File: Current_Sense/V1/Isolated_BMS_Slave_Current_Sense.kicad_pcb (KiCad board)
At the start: 2 copper layers, 0 parts

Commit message: placing power supply
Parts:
- added C201: 885012107015, Capacitors:C0805, F.Cu at (-25.4, -1.42)
- added C202, C205, C209, C301, C305, C306, C510, C514: 885012207098, Capacitors:C0805, F.Cu at (-25.4, -1.42)
- added C203, C204, C208: 885012207102, Capacitors:C0805, F.Cu at (-25.4, -1.42)
- added C206, C207, C302, C303, C310, C311: Capacitor_Generic, Capacitors:C0805, F.Cu at (-25.4, -1.42)
- added C304, C307, C308, C309: 885012207080, Capacitors:C0805, F.Cu at (-25.4, -1.42)
- added C401: C3216X5R1E336M160AC, Capacitors:C1206, B.Cu at (189.1, 68.8)
- added C402: C3216X5R1E336M160AC, Capacitors:C1206, B.Cu at (186.4, 68.8)
- added C403: C3216X5R1E336M160AC, Capacitors:C1206, B.Cu at (183.8, 68.8)
- added C404: C3216X5R1E336M160AC, Capacitors:C1206, F.Cu at (193.0, 93.9)
- added C405: C3216X5R1E336M160AC, Capacitors:C1206, F.Cu at (193.0, 91.1)
- added C406: C3216X5R1E336M160AC, Capacitors:C1206, B.Cu at (193.0, 92.5)
- added C407: C3216X5R1E336M160AC, Capacitors:C1206, B.Cu at (196.5, 84.5)
- added C408: C3216X5R1E336M160AC, Capacitors:C1206, B.Cu at (189.1, 63.3)
- added C409: C3216X5R1E336M160AC, Capacitors:C1206, B.Cu at (186.4, 63.3)
- added C410: C3216X5R1E336M160AC, Capacitors:C1206, B.Cu at (183.8, 63.3)
- added C411: 885012207098, Capacitors:C0805, B.Cu at (188.3, 83.6)
- added C412: 885012107018, Capacitors:C0805, F.Cu at (179.1, 92.6)
- added C413: 885012107018, Capacitors:C0805, F.Cu at (179.1, 90.0)
- added C414: 885012107014, Capacitors:C0805, F.Cu at (179.1, 87.2)
- added C415: 885012107018, Capacitors:C0805, F.Cu at (173.0, 69.8)
- added C416: 885012107018, Capacitors:C0805, F.Cu at (175.5, 69.8)
- added C417: 885012107014, Capacitors:C0805, F.Cu at (166.1, 74.7)
- added C418, C419: 885012107018, Capacitors:C0805, F.Cu at (-25.4, -1.42)
- added C420: 885012107014, Capacitors:C0805, F.Cu at (-25.4, -1.42)
- added C501: 885012007027, Capacitors:C0805, F.Cu at (57.3, 95.6)
- added C502: 885012007027, Capacitors:C0805, F.Cu at (66.2, 97.8)
- added C503: 885012207098, Capacitors:C0805, B.Cu at (71.2, 111.6)
- added C504: 885012107015, Capacitors:C0805, B.Cu at (70.5, 114.2)
- added C505: 885012007053, Capacitors:C0805, F.Cu at (32.3, 103.9)
- added C506: 885012007053, Capacitors:C0805, F.Cu at (32.3, 91.8)
- added C507: 885012207098, Capacitors:C0805, B.Cu at (79.9, 113.1)
- added C508: 885012107015, Capacitors:C0805, B.Cu at (65.7, 118.6)
- added C509: 885012207092, Capacitors:C0805, B.Cu at (68.1, 118.6)
- added C511: 885012107018, Capacitors:C0805, B.Cu at (77.2, 125.6)
- added C512: 885012207098, Capacitors:C0805, B.Cu at (79.2, 123.3)
- added C513: 885012207098, Capacitors:C0805, B.Cu at (71.6, 123.6)
- added C515: 885012007053, Capacitors:C0805, F.Cu at (-25.4, -1.42)
- added D301, D302: D1213A-02SOL-7, IC:SOT-23-3, F.Cu at (-25.4, -1.42)
- added D401: NSR0530HT1G, Diodes:SOD-323, F.Cu at (188.8, 80.2)
- added D501: 150080VS75000, Diodes:LED_0805_GREEN, F.Cu at (66.8, 134.6)
- added D502: 150080YS75000, Diodes:LED_0805_YELLOW, F.Cu at (71.6, 134.5)
- added D503: 150080RS75000, Diodes:LED_0805_RED, F.Cu at (77.1, 134.5)
- added J201: 649002227222, Connectors:649002227222, F.Cu at (47.2, 85.2)
- added J202: 649002227222, Connectors:649002227222, F.Cu at (86.7, 84.8)
- added J301: 649006227222, Connectors:649006227222, F.Cu at (196.1, 110.5)
- added J302: 649006227222, Connectors:649006227222, F.Cu at (175.8, 110.5)
- added J401: Header_Male_Pin_2.54mm_1X2_,_Unshrouded, Connectors:Headers_2.54mm_1X2, F.Cu at (-25.4, -1.42)
- added J501: Header_Male_Pin_2.54mm_1X6_,_Unshrouded, Connectors:Headers_2.54mm_1X6, F.Cu at (-25.4, -1.42)
- added J502: Header_Male_Pin_2.54mm_1X3_,_Unshrouded, Connectors:Headers_2.54mm_1X3, F.Cu at (-25.4, -1.42)
- added L401: LQM31PN4R7M00L, Inductors:I1206, F.Cu at (185.9, 71.4)
- added L402: LQM31PN4R7M00L, Inductors:I1206, F.Cu at (193.0, 88.3)
- added L403: LQM31PN4R7M00L, Inductors:I1206, F.Cu at (186.0, 66.3)
- added R201: RC0805JR-072K2L, Resistors:R0805, F.Cu at (-25.4, -1.42)
- added R202, R203, R213: RC0805JR-0747KL, Resistors:R0805, F.Cu at (-25.4, -1.42)
- added R204: RC0805JR-0733KL, Resistors:R0805, F.Cu at (-25.4, -1.42)
- added R205, R206, R212: RC0805JR-0722RL, Resistors:R0805, F.Cu at (-25.4, -1.42)
- added R207, R210: Resistor_Generic, Capacitors:C0805, F.Cu at (-25.4, -1.42)
- added R208, R209, R211, R302, R303, R305, R306, R504, R506: RC0805JR-07100RL, Resistors:R0805, F.Cu at (-25.4, -1.42)
- added R301, R307: RC0805JR-070RL, Resistors:R0805, F.Cu at (-25.4, -1.42)
- added R304: RC1206JR-07120RL, Resistors:R1206, F.Cu at (-25.4, -1.42)
- added R401: Resistor_Generic, Resistors:R0805, B.Cu at (176.0, 69.8)
- added R402: RC0805JR-071KL, Resistors:R0805, B.Cu at (190.4, 79.0)
- added R403: Resistor_Generic, Resistors:R0805, B.Cu at (176.0, 63.4)
- added R501: RC0805JR-070RL, Resistors:R0805, F.Cu at (61.8, 100.6)
- added R502: RC0805JR-070RL, Resistors:R0805, F.Cu at (40.1, 99.8)
- added R503, R505, R507: RC0805JR-074K7L, Resistors:R0805, F.Cu at (-25.4, -1.42)
- added R508: RC0805JR-07470RL, Resistors:R0805, F.Cu at (66.8, 138.8)
- added R509: RC0805JR-07470RL, Resistors:R0805, F.Cu at (71.6, 138.7)
- added R510: RC0805JR-07470RL, Resistors:R0805, F.Cu at (77.1, 138.7)
- added R511: RC0805JR-071KL, Resistors:R0805, F.Cu at (-25.4, -1.42)
- added SW501: PTS645SM43SMTR92, Switches:PTS645_6X6X4_SMD, F.Cu at (36.4, 135.0)
- added SW502: PTS645SM43SMTR92, Switches:PTS645_6X6X4_SMD, F.Cu at (52.7, 135.3)
- added TP201, TP202, TP203, TP204, TP301, TP302, TP303, TP304, TP407, TP501, TP502, TP503: Test_Point_THM, Connectors:Keystone_5001, F.Cu at (-25.4, -1.42)
- added TP401: Test_Point_THM, Connectors:Keystone_5001, F.Cu at (180.5, 71.9)
- added TP402: Test_Point_THM, Connectors:Keystone_5001, F.Cu at (199.4, 88.3)
- added TP403: Test_Point_THM, Connectors:Keystone_5001, F.Cu at (180.5, 67.7)
- added TP404: Test_Point_THM, Connectors:Keystone_5001, F.Cu at (186.3, 103.1)
- added TP405: Test_Point_THM, Connectors:Keystone_5001, F.Cu at (171.2, 88.4)
- added TP406: Test_Point_THM, Connectors:Keystone_5001, F.Cu at (162.6, 66.0)
- added TP408: Test_Point_THM, Connectors:Keystone_5001, F.Cu at (180.5, 63.4)
- added U201: LM4040CYM3-4.1-TR, IC:SOT-23-3, F.Cu at (-25.4, -1.42)
- added U202: PGA281AIPWR, IC:TSSOP-16, F.Cu at (75.4, 93.6)
- added U203: ADC141S626CIMM/NOPB, IC:VSSOP-10, F.Cu at (74.8, 100.7)
- added U301: SI8422AB-D-IS, IC:SOIC-8, F.Cu at (168.5, 82.8)
- added U302: SN65HVD232DR, IC:SOIC-8, F.Cu at (178.7, 82.9)
- added U401: PQMC3-D12-D15-S, Assembly:PQMC3, F.Cu at (193.2, 84.1)
- added U402: NCP1117LPST33T3G, IC:SOT-223-3, B.Cu at (178.1, 89.9)
- added U403: NCP1117ST50T3G, IC:SOT-223-3, F.Cu at (168.1, 68.8)
- added U404: NCP1117LPST33T3G, IC:SOT-223-3, F.Cu at (175.0, 33.0)
- added U501: STM32F446RE, IC:LQFP-64, F.Cu at (74.0, 117.5)
- added XTAL501: ABS25-32.768KHZ-6-T, Crystals:ABS25, F.Cu at (61.7, 95.0)
- added XTAL502: ABLS-8.000MHZ-D-T, Crystals:HC49_US, F.Cu at (36.1, 96.8)

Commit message: remove NTC, place component on PCB
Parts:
- removed J201: 649002227222, Connectors:649002227222
- C201, C202, C203, C204, C205, C206, C207, C208, C209, C415, C417, C418, C419, C420, R201, R203, R208, R209, R211, R508, R509, R510: moved to B.Cu
- R207, R210: footprint Capacitors:C0805 -> Resistors:R0805
- moved TP302 232.7 mm to (188.7, 89.7), turned to 270 degrees
- moved R304 226.9 mm to (182.6, 89.3)
- moved TP304 224.2 mm to (179.5, 89.7), turned to 270 degrees
- moved C418 204.4 mm to (164.9, 73.4), turned to 180 degrees
- moved C419 203.5 mm to (164.9, 70.9), turned to 180 degrees
- moved R302 202.4 mm to (157.2, 85.9), turned to 90 degrees
- moved R305 198.7 mm to (154.7, 82.5), turned to 270 degrees
- moved C420 195.9 mm to (156.4, 71.6)
- moved TP407 190.8 mm to (153.2, 66.0), turned to 270 degrees
- moved TP201 190.1 mm to (141.0, 90.7)
- moved J401 187.8 mm to (149.9, 66.0), turned to 270 degrees
- moved TP202 187.7 mm to (141.0, 85.6)
- moved C202 185.5 mm to (137.7, 87.1), turned to 180 degrees
- moved U201 185.3 mm to (136.9, 88.1), turned to 270 degrees
- moved R211 184.8 mm to (132.6, 94.5), turned to 270 degrees
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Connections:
- U501 pad 14: /NTC_ADC -> /STM32F446/PA0
- U501 pad 15: /NTC_GPIO -> /STM32F446/PA1

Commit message: routing uC
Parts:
- removed R204: RC0805JR-0733KL, Resistors:R0805
- removed TP203, TP204, TP501, TP502, TP503: Test_Point_THM, Connectors:Keystone_5001
- C301, C302, C303, C304, C305, C306, C308, C309, C310, C311, C510, C515, D301, D302, R306: moved to B.Cu
- R208, R209, R211: moved to F.Cu
- moved C303 283.8 mm to (191.1, 112.5)
- moved C310 273.7 mm to (177.2, 112.8), turned to 180 degrees
- moved C307 251.9 mm to (166.1, 78.9)
- moved C302 248.7 mm to (202.2, 112.5), turned to 180 degrees
- moved D301 244.8 mm to (196.8, 113.6)
- moved C309 241.1 mm to (166.1, 78.9)
- moved C304 240.7 mm to (157.7, 87.4), turned to 270 degrees
- moved R301 240.0 mm to (191.9, 100.5), turned to 180 degrees
- moved C308 239.2 mm to (154.9, 89.4), turned to 90 degrees
- moved D302 234.6 mm to (171.6, 114.0)
- moved C311 223.0 mm to (166.2, 112.8)
- moved R307 217.6 mm to (167.0, 100.3), turned to 90 degrees
- moved R303 213.8 mm to (170.8, 83.6), turned to 90 degrees
- moved R306 213.3 mm to (170.8, 82.4), turned to 270 degrees
- moved TP301 206.3 mm to (160.8, 87.6), turned to 270 degrees
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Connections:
- D302 pad 1: /Communication Interface/CAN_P -> /Communication Interface/CAN_N
- D302 pad 2: /Communication Interface/CAN_N -> /Communication Interface/CAN_P
- J302 pad 3: /Communication Interface/Shield1 -> /Communication Interface/Shield2
- J302 pad 6: /Communication Interface/Shield1 -> /Communication Interface/Shield2
- R307 pad 1: /Communication Interface/Shield1 -> /Communication Interface/Shield2
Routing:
- net /STM32F446/NRST: track 0.00 -> 110.0 mm, vias 0 -> 1
- net /Communication Interface/CAN_P: track 0.00 -> 103.9 mm, vias 0 -> 2
- net /Communication Interface/CAN_N: track 0.00 -> 94.4 mm, vias 0 -> 2
- net /STM32F446/PA3: track 0.00 -> 51.6 mm
- net /STM32F446/PA2: track 0.00 -> 50.4 mm
- net 12VA: track 0.00 -> 45.8 mm, vias 0 -> 1
- net /Current Sense/EF: track 0.00 -> 43.4 mm
- net /Current Sense/G4: track 0.00 -> 40.5 mm
- net 3.3VA: track 0.00 -> 40.2 mm, vias 0 -> 1
- net /Current Sense/G3: track 0.00 -> 38.8 mm
- net /STM32F446/USER_BTN: track 0.00 -> 38.7 mm, vias 0 -> 2
- net /Current Sense/G2: track 0.00 -> 37.3 mm
- net /STM32F446/SWDIO: track 0.00 -> 36.3 mm, vias 0 -> 2
- net /Current Sense/G1: track 0.00 -> 35.8 mm
- net /Current Sense/G0: track 0.00 -> 34.1 mm
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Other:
- board outline added: 96.5 x 62.2 mm
- net class Default: via_dia 0.6858 -> 1.016
- rule via_min_size: 0.6858 -> 1.016

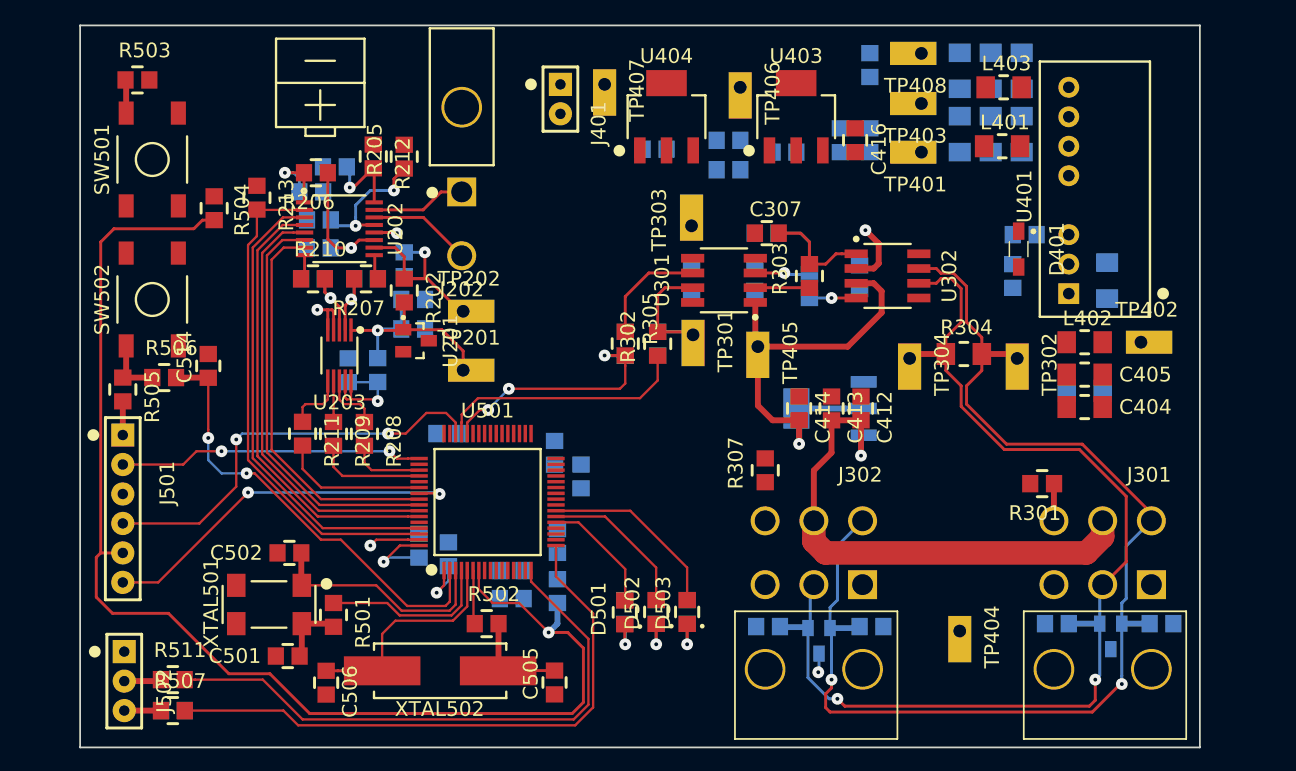
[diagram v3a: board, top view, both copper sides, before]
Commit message: board done, DRC clean
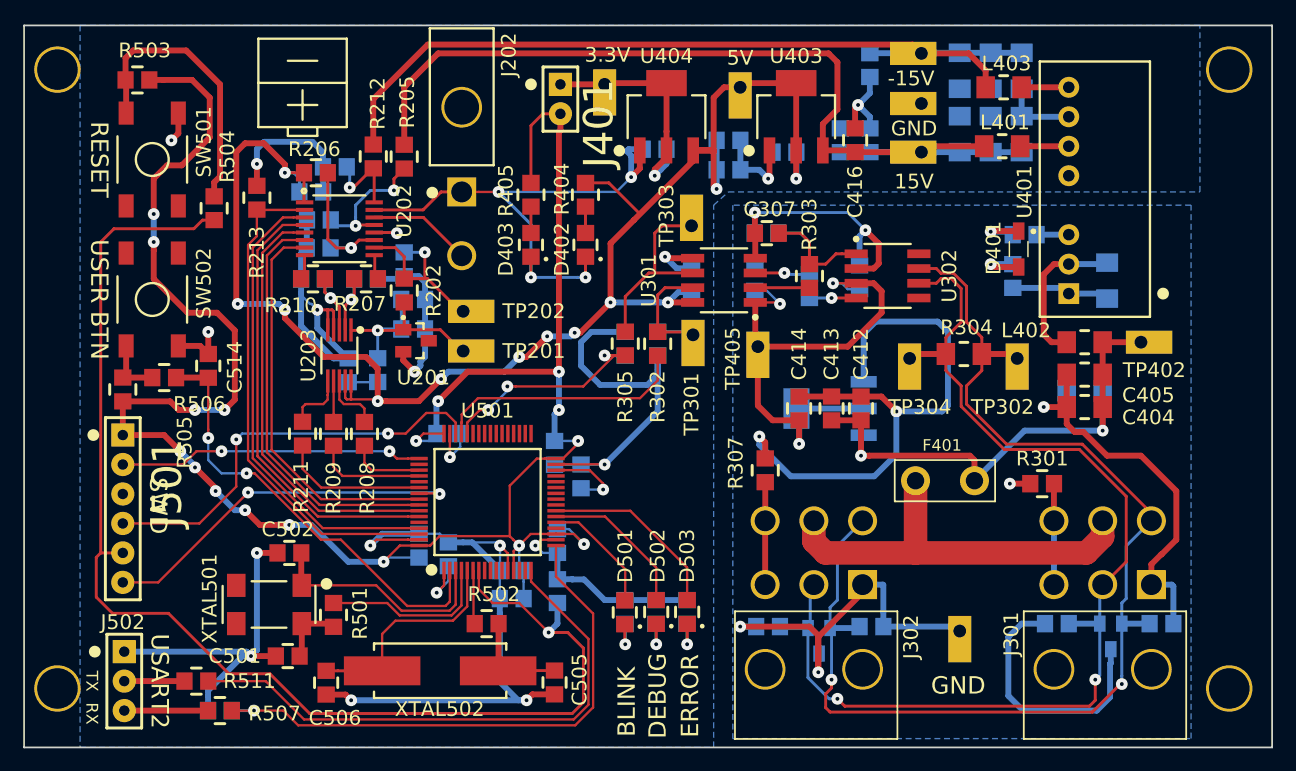
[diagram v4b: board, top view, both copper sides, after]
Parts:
- added D402: 150080VS75000, Diodes:LED_0805_GREEN, F.Cu at (151.5, 80.9)
- added D403: 150080VS75000, Diodes:LED_0805_GREEN, F.Cu at (146.8, 80.9)
- added F401: 39511000440, Fuses:TE5_395, F.Cu at (182.5, 100.2)
- added R404: RC0805JR-07470RL, Resistors:R0805, F.Cu at (151.5, 76.6)
- added R405: RC0805JR-07470RL, Resistors:R0805, F.Cu at (146.8, 76.6)
- added REF**: Mounting_Hole_3mm, Connectors:Mounting_Hole_3mm, F.Cu at (207.0, 64.8)
- added REF**: Mounting_Hole_3mm, Connectors:Mounting_Hole_3mm, F.Cu at (207.0, 118.1)
- added REF**: Mounting_Hole_3mm, Connectors:Mounting_Hole_3mm, F.Cu at (106.0, 120.0)
- added REF**: Mounting_Hole_3mm, Connectors:Mounting_Hole_3mm, F.Cu at (105.7, 111.6)
- moved R507 4.06 mm to (119.0, 120.0)
- moved C515 4.05 mm to (119.0, 120.0)
- moved R511 2.04 mm to (116.9, 117.5)
- moved TP201 1.65 mm to (141.0, 89.0)
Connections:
- J301 pad 5: 12VA -> CAN_PWR
- J302 pad 5: 12VA -> CAN_PWR
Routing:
- net DGND: track 19.4 -> 288.7 mm, vias 3 -> 22
- net GNDA: track 7.10 -> 179.5 mm, vias 2 -> 8
- net VDD: track 9.74 -> 181.2 mm, vias 1 -> 17
- net 5VB: track 17.0 -> 143.1 mm, vias 2 -> 12
- net 15VB: track 0.00 -> 81.7 mm
- net -15VB: track 0.00 -> 74.1 mm
- net CAN_PWR: track 0.00 -> 35.2 mm
- net Net-(R503-Pad1): track 2.88 -> 24.3 mm
- net Net-(C420-Pad2): track 0.00 -> 20.3 mm, vias 0 -> 1
- net Net-(C407-Pad2): track 0.00 -> 13.3 mm
- net 3.3VA: track 40.2 -> 49.5 mm, vias 1 -> 3
- net /Communication Interface/Shield2: track 0.00 -> 8.83 mm
- net Net-(C511-Pad2): track 0.00 -> 7.01 mm, vias 0 -> 1
- net /Communication Interface/uC_CAN_RX: track 9.68 -> 16.5 mm
- net /Communication Interface/Shield1: track 3.21 -> 8.71 mm
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- added copper zone on B.Cu, net DGND
- added copper zone on B.Cu, net GNDA
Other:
- board size 96.5 x 62.2 mm -> 107.6 x 62.2 mm
- net class Default: clearance 0.2032 -> 0.1524
- rule trace_clearance: 0.2032 -> 0.1524
- board text added: "-15V"
- board text added: "15V"
- board text added: "3.3V"
- board text added: "5V"
- board text added: "BLINK"
- board text added: "DEBUG"
- board text added: "ERROR"
- board text added: "GND"
- board text added: "RESET"
- board text added: "RX"
- board text added: "SWD"
- board text added: "TX"
- board text added: "USART2"
- board text added: "USER BTN"
